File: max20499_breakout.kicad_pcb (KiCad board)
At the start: 2 copper layers, 1 part, among them U1 MAX20499

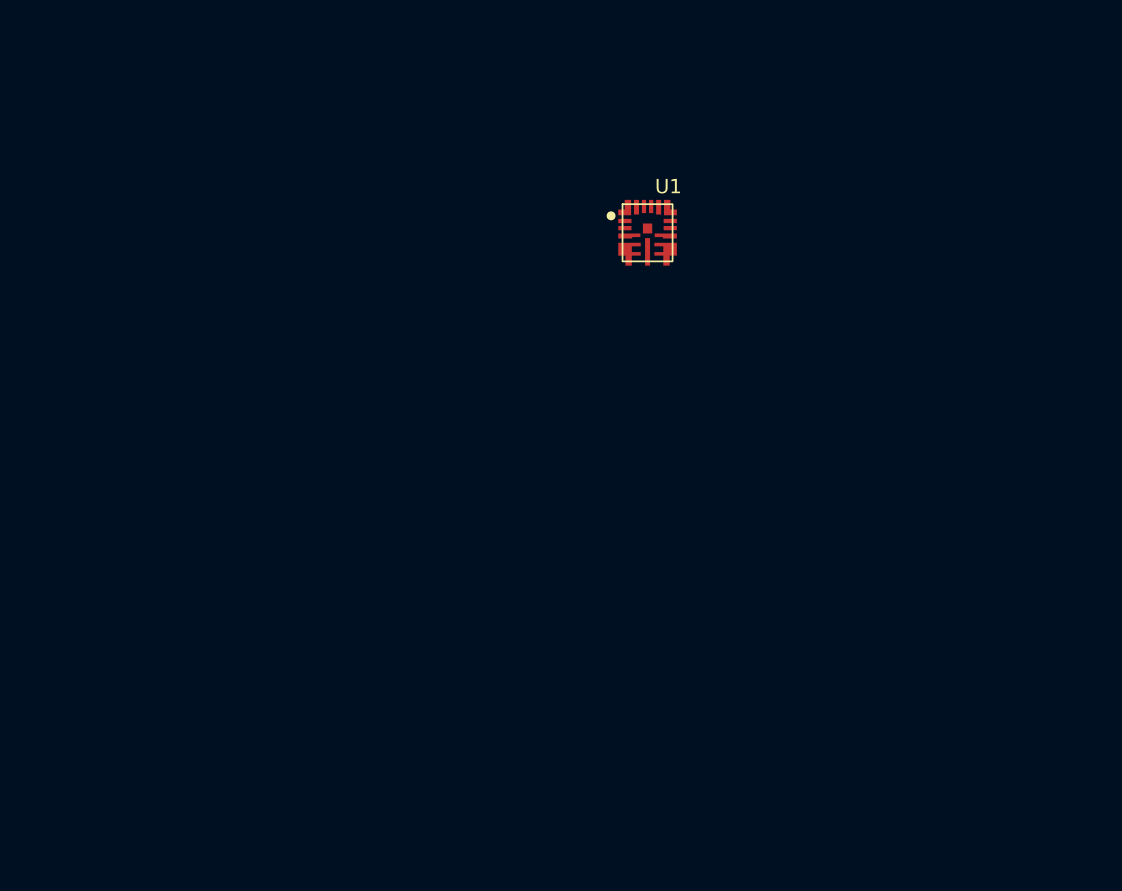
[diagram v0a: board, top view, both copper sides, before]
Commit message: finished schematic capture. started organizing PCB
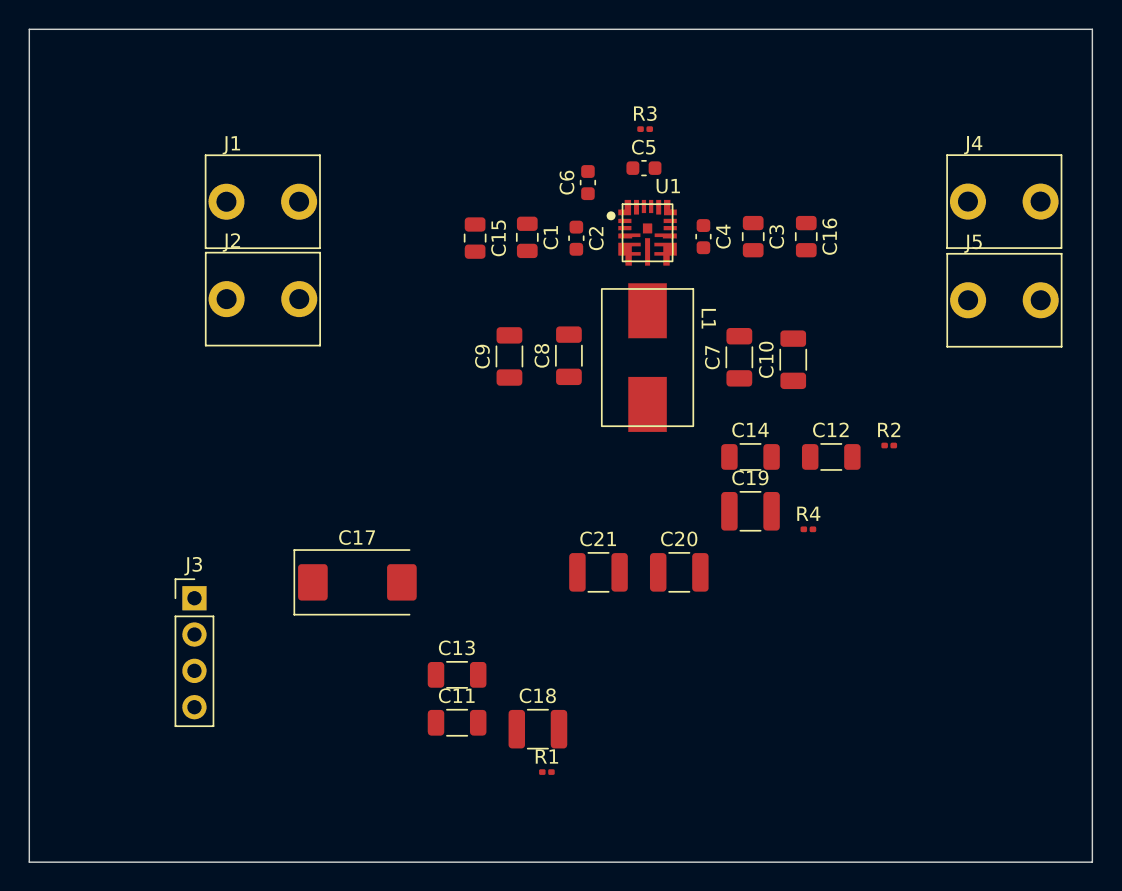
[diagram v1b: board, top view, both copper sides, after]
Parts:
- added C1: 10uF, Capacitor_SMD:C_0805_2012Metric, F.Cu at (123.1, 93.6)
- added C10: 47uF, Capacitor_SMD:C_1206_3216Metric, F.Cu at (141.7, 102.2)
- added C11: 47uF, Capacitor_SMD:C_1206_3216Metric, F.Cu at (118.2, 127.5)
- added C12: 47uF, Capacitor_SMD:C_1206_3216Metric, F.Cu at (144.4, 109.0)
- added C13: 47uF, Capacitor_SMD:C_1206_3216Metric, F.Cu at (118.2, 124.2)
- added C14: 47uF, Capacitor_SMD:C_1206_3216Metric, F.Cu at (138.7, 109.0)
- added C15: 10uF, Capacitor_SMD:C_0805_2012Metric, F.Cu at (119.5, 93.7)
- added C16: 10uF, Capacitor_SMD:C_0805_2012Metric, F.Cu at (142.6, 93.5)
- added C17: 470uF, Capacitor_Tantalum_SMD:CP_EIA-7343-43_Kemet-X, F.Cu at (111.2, 117.7)
- added C18: 47uF, Capacitor_SMD:C_1210_3225Metric, F.Cu at (123.9, 128.0)
- added C19: 47uF, Capacitor_SMD:C_1210_3225Metric, F.Cu at (138.7, 112.8)
- added C2: 1uF, Capacitor_SMD:C_0603_1608Metric, F.Cu at (126.5, 93.7)
- added C20: 47uF, Capacitor_SMD:C_1210_3225Metric, F.Cu at (133.8, 117.0)
- added C21: 47uF, Capacitor_SMD:C_1210_3225Metric, F.Cu at (128.1, 117.0)
- added C3: 10uF, Capacitor_SMD:C_0805_2012Metric, F.Cu at (138.9, 93.5)
- added C4: 1uF, Capacitor_SMD:C_0603_1608Metric, F.Cu at (135.4, 93.5)
- added C5: 2.2uF, Capacitor_SMD:C_0603_1608Metric, F.Cu at (131.3, 88.8)
- added C6: 0.1uF, Capacitor_SMD:C_0603_1608Metric, F.Cu at (127.4, 89.8)
- added C7: 47uF, Capacitor_SMD:C_1206_3216Metric, F.Cu at (137.9, 102.0)
- added C8: 47uF, Capacitor_SMD:C_1206_3216Metric, F.Cu at (126.0, 101.9)
- added C9: 47uF, Capacitor_SMD:C_1206_3216Metric, F.Cu at (121.9, 101.9)
- added J1: Conn_01x01, low_voltage_reg:63862-1, F.Cu at (104.6, 91.1)
- added J2: Conn_01x01, low_voltage_reg:63862-1, F.Cu at (104.6, 97.9)
- added J3: Conn_01x04, Connector_PinHeader_2.54mm:PinHeader_1x04_P2.54mm_Vertical, F.Cu at (99.8, 118.8)
- added J4: Conn_01x01, low_voltage_reg:63862-1, F.Cu at (156.5, 91.1)
- added J5: Conn_01x01, low_voltage_reg:63862-1, F.Cu at (156.5, 98.0)
- added L1: 70nH, low_voltage_reg:VLBU9664100LT-R07M, F.Cu at (131.5, 102.0)
- added R1: 1K, Resistor_SMD:R_0201_0603Metric, F.Cu at (124.5, 131.0)
- added R2: 1K, Resistor_SMD:R_0201_0603Metric, F.Cu at (148.4, 108.2)
- added R3: 2.2, Resistor_SMD:R_0201_0603Metric, F.Cu at (131.4, 86.0)
- added R4: 10K, Resistor_SMD:R_0201_0603Metric, F.Cu at (142.8, 114.0)
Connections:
- U1 pad 1: unconnected-(U1-Pad1) -> /VIN
- U1 pad 10: unconnected-(U1-Pad10) -> GND
- U1 pad 11: unconnected-(U1-Pad11) -> /VOUT
- U1 pad 12: unconnected-(U1-Pad12) -> GND
- U1 pad 13: unconnected-(U1-Pad13) -> Net-(R4-Pad2)
- U1 pad 14: unconnected-(U1-Pad14) -> GND
- U1 pad 15: unconnected-(U1-Pad15) -> Net-(U1-Pad15)
- U1 pad 16: unconnected-(U1-Pad16) -> Net-(U1-Pad16)
- U1 pad 17: unconnected-(U1-Pad17) -> Net-(U1-Pad17)
- U1 pad 3: Net-(U1-Pad3) -> /VIN
- U1 pad 4: Net-(U1-Pad4) -> GND
- U1 pad 5: Net-(U1-Pad4) -> GND
- U1 pad 6: unconnected-(U1-Pad6) -> Net-(U1-Pad6)
- U1 pad 7: Net-(U1-Pad4) -> GND
- U1 pad 9: Net-(U1-Pad3) -> /VIN
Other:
- board outline added: 74.3 x 58.3 mm

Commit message: routed PCB
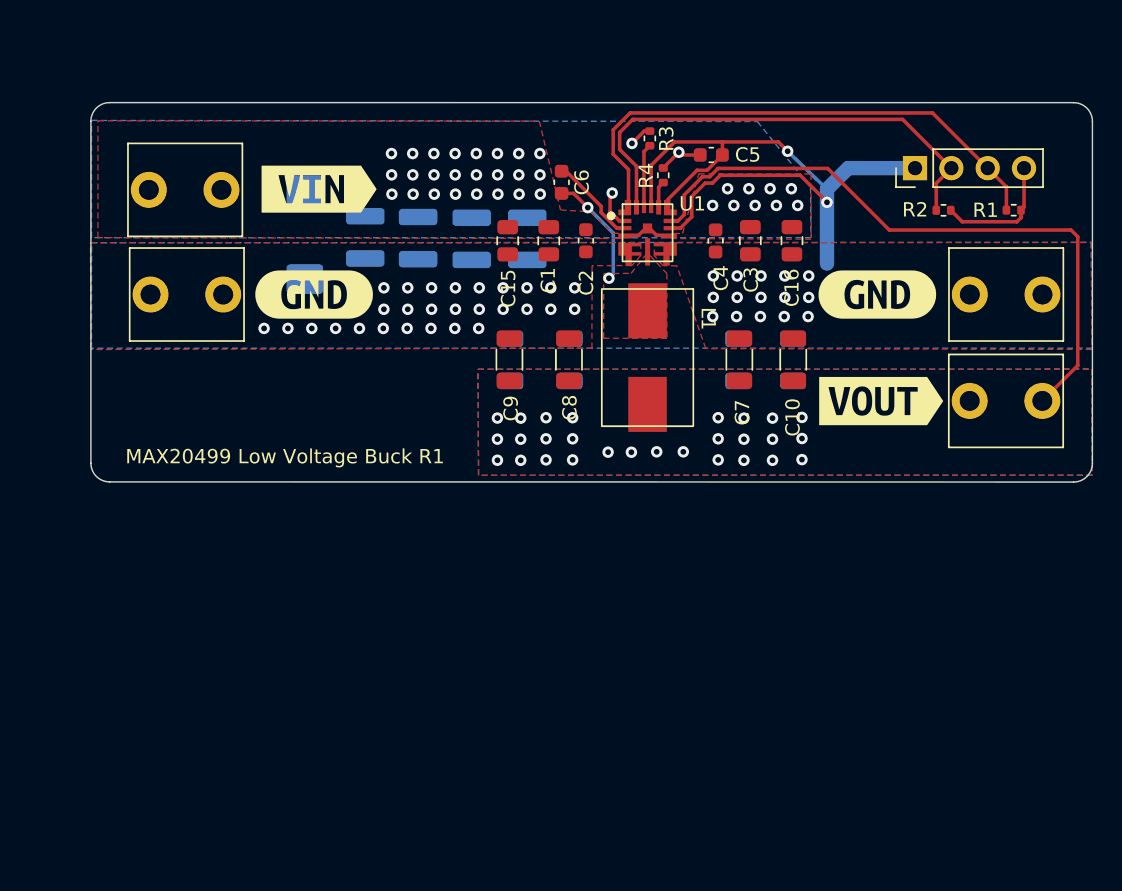
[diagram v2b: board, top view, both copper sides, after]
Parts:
- added kibuzzard-62A80E9C: G***, kibuzzard-62A80E9C, F.Cu at (147.9, 105.0)
- added kibuzzard-62A80EF8: G***, kibuzzard-62A80EF8, F.Cu at (147.6, 97.6)
- added kibuzzard-62A80EF8: G***, kibuzzard-62A80EF8, F.Cu at (108.2, 97.6)
- added kibuzzard-62A80F52: G***, kibuzzard-62A80F52, F.Cu at (108.6, 90.2)
- C11, C12, C13, C14, C17, C18, C19, C20, C21: moved to B.Cu
- R1, R2, R3, R4: footprint Resistor_SMD:R_0201_0603Metric -> Resistor_SMD:R_0402_1005Metric
- moved J3 58.7 mm to (150.2, 88.8), turned to 90 degrees
- moved R1 51.1 mm to (157.1, 91.7), turned to 180 degrees
- moved C18 36.5 mm to (111.8, 93.6), turned to -90 degrees
- moved C11 34.6 mm to (141.7, 102.2), turned to 90 degrees
- moved C19 30.1 mm to (115.5, 93.7), turned to -90 degrees
- moved C13 29.5 mm to (137.9, 102.2), turned to 90 degrees
- moved C20 27.5 mm to (119.2, 93.7), turned to -90 degrees
- moved R4 26.8 mm to (132.6, 89.3), turned to -90 degrees
- moved C17 24.6 mm to (107.6, 93.4), turned to -90 degrees
- moved C21 23.9 mm to (123.1, 93.7), turned to -90 degrees
- moved C12 23.4 mm to (121.9, 102.2), turned to 90 degrees
- moved R2 16.9 mm to (152.2, 91.7), turned to 180 degrees
- moved C14 14.3 mm to (126.1, 102.2), turned to 90 degrees
- moved J4 13.9 mm to (156.6, 105.0)
- moved J2 9.38 mm to (99.2, 90.3)
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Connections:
- net Net-(U1-Pad16) renamed /SDA
- net Net-(U1-Pad17) renamed /SCL
- net Net-(U1-Pad6) renamed /LX1
- U1 pad EP: (no net) -> /VIN
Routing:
- net GND: track 0.00 -> 49.3 mm, vias 0 -> 45
- net /VOUT: track 0.00 -> 45.3 mm, vias 0 -> 28
- net /SCL: track 0.00 -> 37.1 mm
- net /SDA: track 0.00 -> 34.1 mm
- net Net-(J3-Pad4): track 0.00 -> 8.91 mm
- net /VIN: track 0.00 -> 8.69 mm, vias 0 -> 36
- net /LX1: track 0.00 -> 8.04 mm, vias 0 -> 2
- net Net-(C6-Pad1): track 0.00 -> 6.32 mm
- net Net-(R3-Pad2): track 0.00 -> 4.42 mm
- net Net-(R4-Pad2): track 0.00 -> 1.86 mm
- added copper zone on F.Cu, net /LX1
- added copper zone on B.Cu, net /VIN
- added copper zone on F.Cu, net /VIN
- added copper zone on B.Cu, net /VOUT
- added copper zone on F.Cu, net /VOUT
- added copper zone on B.Cu, net GND
- added copper zone on F.Cu, net GND
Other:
- board size 74.3 x 58.3 mm -> 70 x 26.5 mm
- board text added: "GND"
- board text added: "MAX20499 Low Voltage Buck R1"
- board text added: "SCL"
- board text added: "SDA"
- board text added: "VPU"

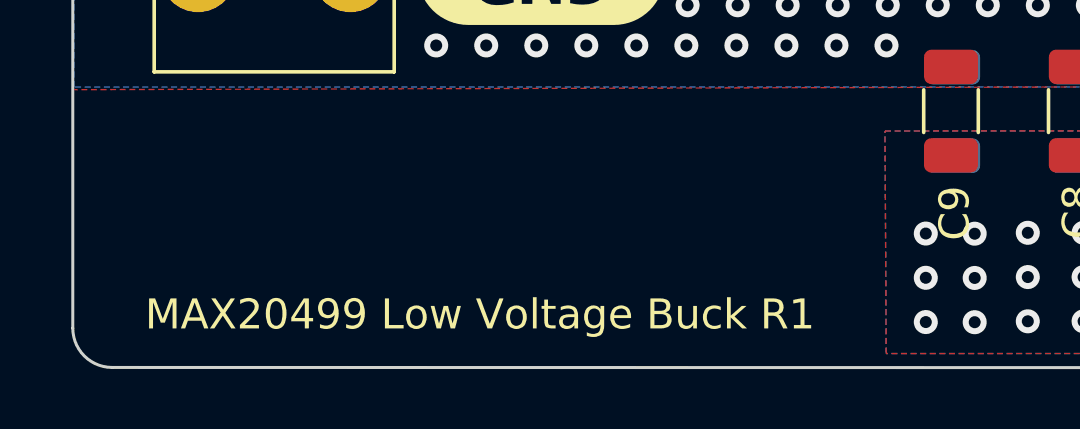
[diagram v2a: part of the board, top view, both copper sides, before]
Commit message: added DK part numbers in schematic
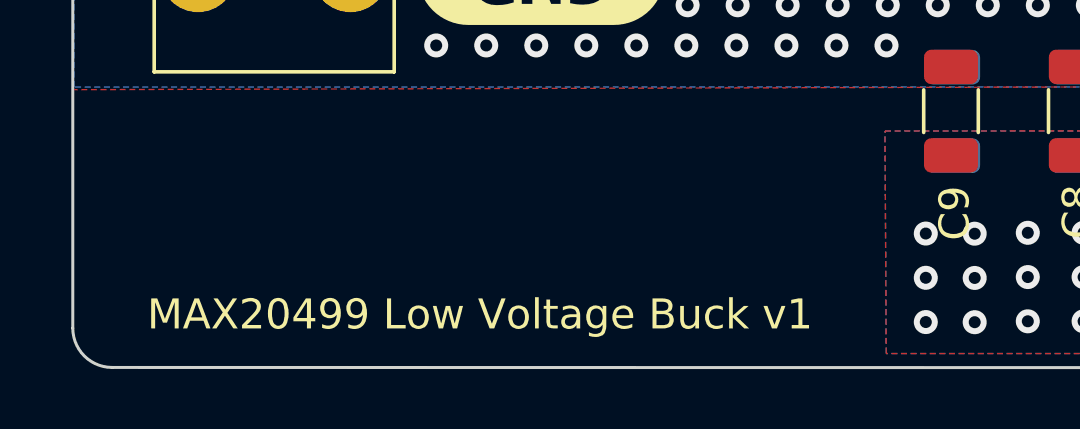
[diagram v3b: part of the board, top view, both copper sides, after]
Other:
- board text added: "MAX20499 Low Voltage Buck v1"
- board text removed: "MAX20499 Low Voltage Buck R1"
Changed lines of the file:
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@@
     (effects (font (size 1 1) (thickness 0.15)) (justify mirror))
   )
-  (gr_text "MAX20499 Low Voltage Buck R1" (at 106.17 108.94) (layer "F.SilkS")
+  (gr_text "MAX20499 Low Voltage Buck v1" (at 106.17 108.94) (layer "F.SilkS")
     (effects (font (size 1 1) (thickness 0.15)))
   )

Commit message: lil' silkscreen tweak. regenerated gerbers
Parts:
- moved J1 0.12 mm to (99.2, 97.6)
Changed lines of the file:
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@@
   (net 10 "/SCL")
   (footprint "low_voltage_reg:63862-1" (layer "F.Cu")
-    (at 99.31 97.6)
+    (at 99.19 97.6)
     (property "Sheetfile" "max20499_breakout.kicad_sch")
     (property "Sheetname" "")
@@
   )
   (footprint "low_voltage_reg:63862-1" (layer "F.Cu")
-    (at 156.61 97.6)
-    (property "Sheetfile" "max20499_breakout.kicad_sch")
-    (property "Sheetname" "")
+    (at 156.6 97.6)
+    (property "Sheetfile" "max20499_breakout.kicad_sch")
+    (property "Sheetname" "")
